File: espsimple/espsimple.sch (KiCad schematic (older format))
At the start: 13 parts, among them J1 Conn_01x02_Female, J2 Conn_01x08, J3 Conn_01x08, SW1 SW_Push, U1 ESP-12F, U2 AMS1117-3.3

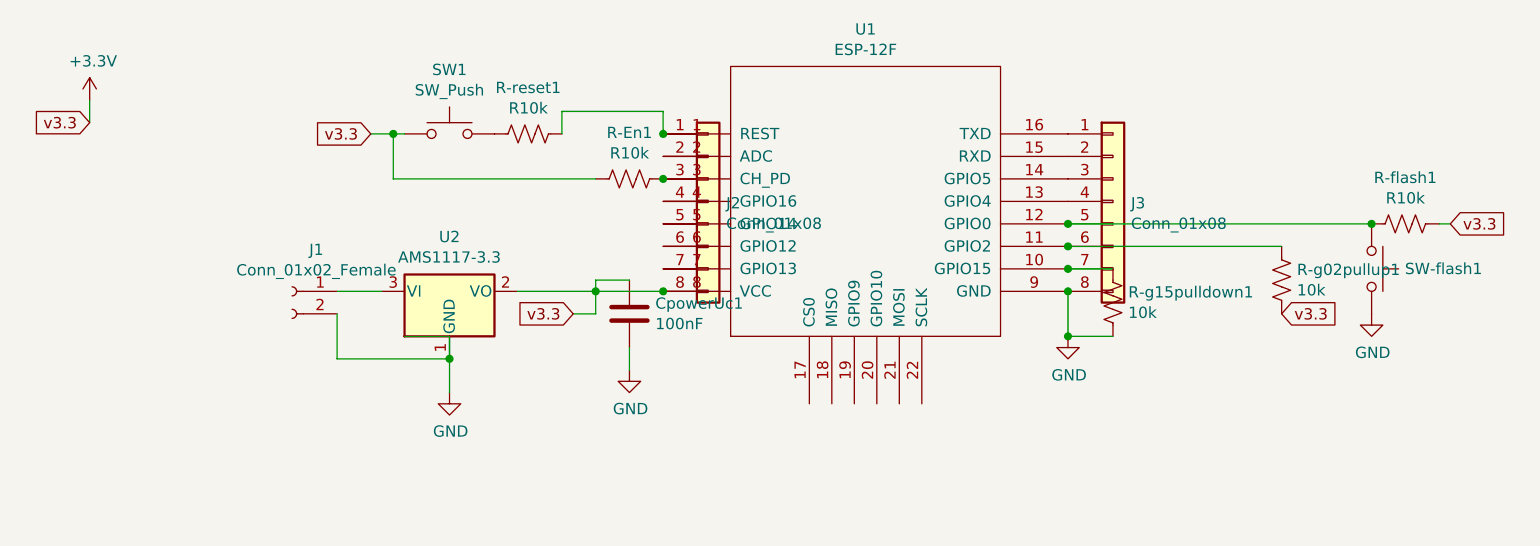
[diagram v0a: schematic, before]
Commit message: finish board for esp12
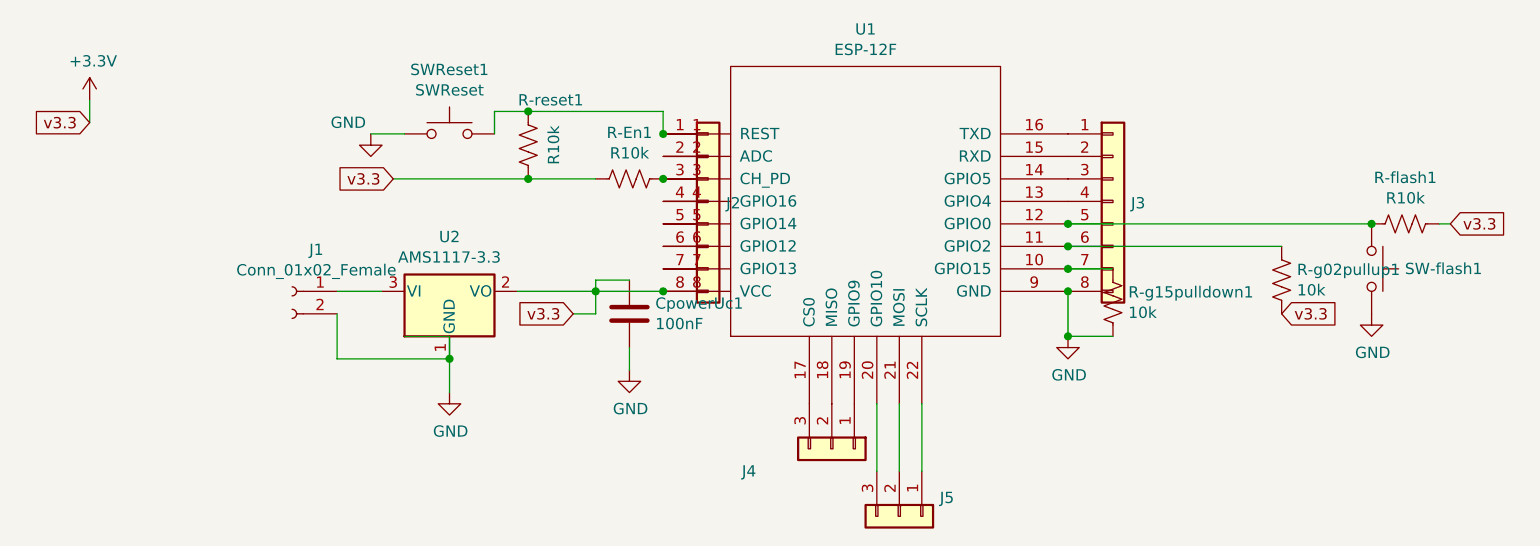
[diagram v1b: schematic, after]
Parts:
- added J4, J5: conn1x3, Connector_PinHeader_2.54mm:PinHeader_1x03_P2.54mm_Vertical, symbol Connector_Generic:Conn_01x03
- J2, J3: value Conn_01x08 -> (none)
- SW-flash1: value SW_Push -> SWflash; footprint Package_DIP:DIP-4_W7.62mm -> Button_Switch_THT:SW_PUSH_6mm
- SWReset1: renamed from SW1; value SW_Push -> SWReset; footprint Package_DIP:DIP-4_W7.62mm -> Button_Switch_THT:SW_PUSH_6mm
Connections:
- wire segments 27 -> 30
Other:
- moved on the sheet: R-reset1
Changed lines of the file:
@@
 L Device:R_US R-reset1
 U 1 1 5FD723C5
-P 2750 2600
-F 0 "R-reset1" V 2545 2600 50  0000 C CNN
-F 1 "R10k" V 2636 2600 50  0000 C CNN
-F 2 "Resistor_SMD:R_0805_2012Metric" V 2790 2590 50  0001 C CNN
-F 3 "~" H 2750 2600 50  0001 C CNN
-	1    2750 2600
-	0    1    1    0
-$EndComp
-$Comp
-L Switch:SW_Push SW1
+P 2750 2650
+F 0 "R-reset1" H 2650 2450 50  0000 C CNN
+F 1 "R10k" V 2636 2650 50  0000 C CNN
+F 2 "Resistor_SMD:R_0805_2012Metric" V 2790 2640 50  0001 C CNN
+F 3 "~" H 2750 2650 50  0001 C CNN
+	1    2750 2650
+	-1   0    0    1
+$EndComp
+$Comp
+L Switch:SW_Push SWReset1
 U 1 1 5FD7C06A
 P 2400 2600
-F 0 "SW1" H 2400 2885 50  0000 C CNN
-F 1 "SW_Push" H 2400 2794 50  0000 C CNN
-F 2 "Package_DIP:DIP-4_W7.62mm" H 2400 2800 50  0001 C CNN
+F 0 "SWReset1" H 2400 2885 50  0000 C CNN
+F 1 "SWReset" H 2400 2794 50  0000 C CNN
+F 2 "Button_Switch_THT:SW_PUSH_6mm" H 2400 2800 50  0001 C CNN
 F 3 "~" H 2400 2800 50  0001 C CNN
 	1    2400 2600
@@
 Wire Wire Line
 	3350 2600 3350 2500
-Wire Wire Line
-	3350 2500 2900 2500
-Wire Wire Line
-	2900 2500 2900 2600
-Text GLabel 2050 2600 0    50   Input ~ 0
-v3.3
-Wire Wire Line
-	2050 2600 2150 2600
-Wire Wire Line
-	3050 2800 2150 2800
-Wire Wire Line
-	2150 2800 2150 2600
-Connection ~ 2150 2600
-Wire Wire Line
-	2150 2600 2200 2600
+Text GLabel 2150 2800 0    50   Input ~ 0
+v3.3
+Wire Wire Line
+	3050 2800 2750 2800
 $Comp
 L Device:C CpowerUc1
@@
 P 6500 3200
 F 0 "SW-flash1" V 6500 3348 50  0000 L CNN
-F 1 "SW_Push" V 6545 3348 50  0001 L CNN
-F 2 "Package_DIP:DIP-4_W7.62mm" H 6500 3400 50  0001 C CNN
+F 1 "SWflash" V 6545 3348 50  0001 L CNN
+F 2 "Button_Switch_THT:SW_PUSH_6mm" H 6500 3400 50  0001 C CNN
 F 3 "~" H 6500 3400 50  0001 C CNN
 	1    6500 3200
@@
 P 3550 2900
 F 0 "J2" H 3630 2892 50  0000 L CNN
-F 1 "Conn_01x08" H 3630 2801 50  0000 L CNN
+F 1 " " H 3630 2801 50  0001 L CNN
 F 2 "Connector_PinHeader_2.54mm:PinHeader_1x08_P2.54mm_Vertical" H 3550 2900 50  0001 C CNN
 F 3 "~" H 3550 2900 50  0001 C CNN
@@
 P 5350 2900
 F 0 "J3" H 5430 2892 50  0000 L CNN
-F 1 "Conn_01x08" H 5430 2801 50  0000 L CNN
+F 1 " " H 5430 2801 50  0001 L CNN
 F 2 "Connector_PinHeader_2.54mm:PinHeader_1x08_P2.54mm_Vertical" H 5350 2900 50  0001 C CNN
 F 3 "~" H 5350 2900 50  0001 C CNN
@@
 Connection ~ 5150 3200
 Connection ~ 5150 3300
+$Comp
+L Connector_Generic:Conn_01x03 J4
+U 1 1 5FDA0B08
+P 4100 4000
+F 0 "J4" V 4200 3600 50  0000 L CNN
+F 1 "conn1x3" V 4300 3600 50  0001 L CNN
+F 2 "Connector_PinHeader_2.54mm:PinHeader_1x03_P2.54mm_Vertical" H 4100 4000 50  0001 C CNN
+F 3 "~" H 4100 4000 50  0001 C CNN
+	1    4100 4000
+	0    1    1    0
+$EndComp
+$Comp
+L Connector_Generic:Conn_01x03 J5
+U 1 1 5FDA15FD
+P 4400 4300
+F 0 "J5" V 4318 4480 50  0000 L CNN
+F 1 "conn1x3" V 4363 4480 50  0001 L CNN
+F 2 "Connector_PinHeader_2.54mm:PinHeader_1x03_P2.54mm_Vertical" H 4400 4300 50  0001 C CNN
+F 3 "~" H 4400 4300 50  0001 C CNN
+	1    4400 4300
+	0    1    1    0
+$EndComp
+Wire Wire Line
+	4300 4100 4300 3800
+Wire Wire Line
+	4400 3800 4400 4100
+Wire Wire Line
+	4500 4100 4500 3800
+Wire Wire Line
+	2050 2600 2200 2600
+Connection ~ 2750 2800
+Wire Wire Line
+	2750 2800 2150 2800
+Wire Wire Line
+	2750 2500 3350 2500
+Wire Wire Line
+	2600 2600 2600 2500
+Wire Wire Line
+	2600 2500 2750 2500
+Connection ~ 2750 2500
+$Comp
+L power:GND #PWR?
+U 1 1 5FD956EB
+P 2050 2600
+F 0 "#PWR?" H 2050 2350 50  0001 C CNN
+F 1 "GND" H 1950 2650 50  0000 C CNN
+F 2 "" H 2050 2600 50  0001 C CNN
+F 3 "" H 2050 2600 50  0001 C CNN
+	1    2050 2600
+	1    0    0    -1
+$EndComp
 $EndSCHEMATC
